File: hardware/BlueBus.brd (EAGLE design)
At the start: 90 x 60 mm, 130 parts, among them Q1 NMOSFET-BSS138K, Q2 PMOSFET-DMP1045UQ, Q3 NMOSFET-BSS138K, X1 CRYSTAL-12MHZ

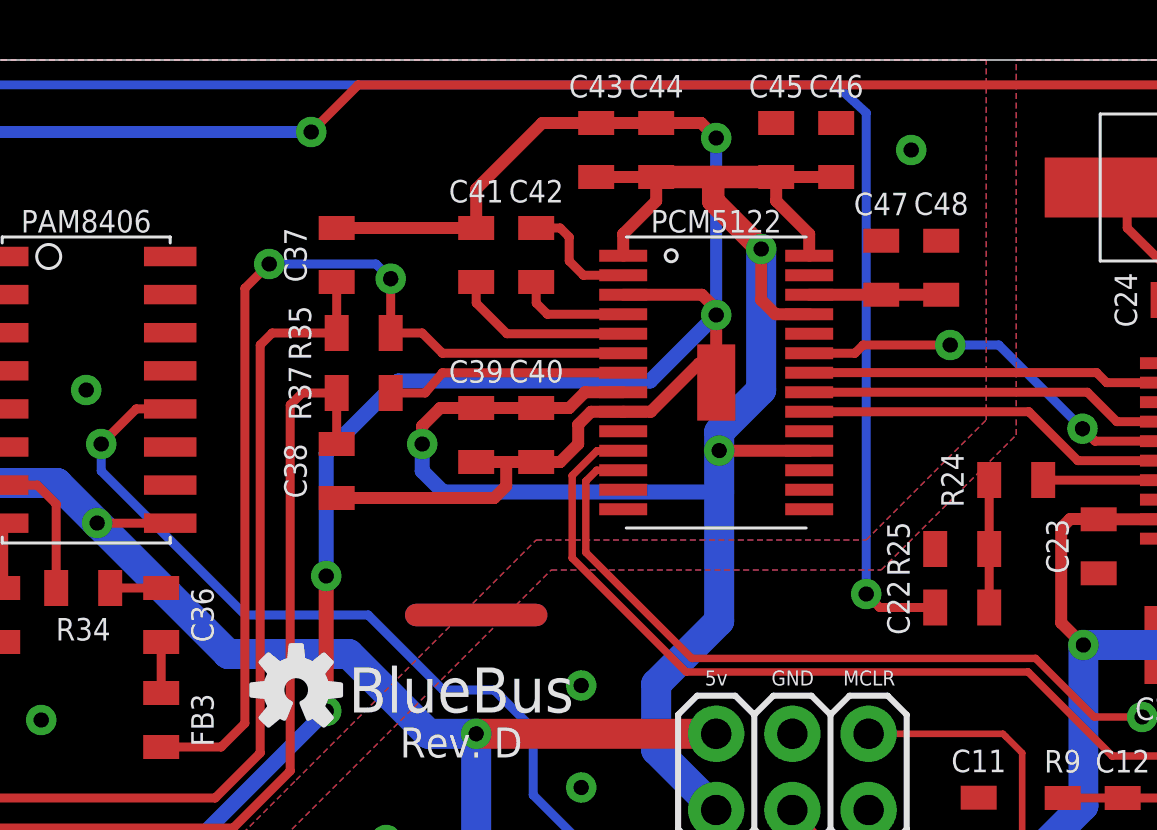
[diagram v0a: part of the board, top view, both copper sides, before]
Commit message: [IMP] hardware: Revision D.1 * Remove errant layers
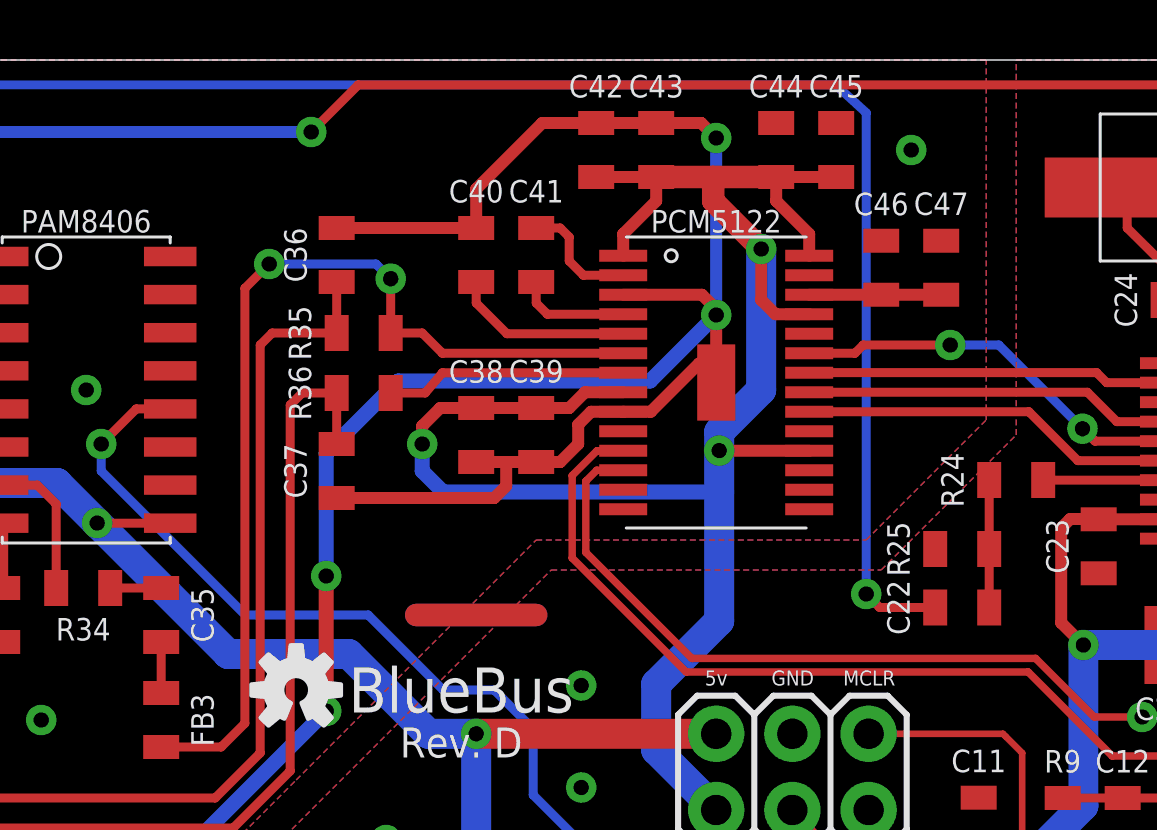
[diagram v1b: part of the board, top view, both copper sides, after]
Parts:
- removed C48: 10uF, Passives:0805
- added C35: 1uF, Passives:0805
- C36: value 1uF -> 9nF
- C38: value 9nF -> 10uF
- C39, C43, C46: value 10uF -> 0.1uF
- C40: value 0.1uF -> 2.2uF
- C42: value 2.2uF -> 10uF
- C45, C47: value 0.1uF -> 10uF
- moved C36 13.4 mm to (29.4, 53.5)
- moved C37 7.20 mm to (29.4, 46.3), turned to 270 degrees
- moved C40 6.32 mm to (34.0, 53.5)
- moved C38 4.80 mm to (34.0, 47.5)
- moved C46 4.20 mm to (47.5, 53.1)
- moved C42 4.03 mm to (38.0, 57.0), turned to 90 degrees
- moved C44 4.00 mm to (44.0, 57.0)
- moved C39 2.00 mm to (36.0, 47.5)
- moved C41 2.00 mm to (36.0, 53.5)
- moved C43 2.00 mm to (40.0, 57.0)
- moved C45 2.00 mm to (46.0, 57.0)
- moved C47 2.00 mm to (49.5, 53.1)
- renumbered R37 to R36
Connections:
- net 3.3V: now also C38.1, C42.1; no longer C40.1, C46.1
- net AGND: now also C36.2, C40.1, C42.2; no longer C40.2, C41.1, C44.2
- net DAC_CAPM: now also C41.2; no longer C42.2
- net DAC_CAPP: now also C41.1; no longer C42.1
- net DAC_LDOO: now also C46.1; no longer C48.1
- net DAC_VNEG: now also C40.2; no longer C41.2
- net GND: now also C44.2; no longer C48.2
- net SPKR_OUT_L: now also C36.1; no longer C37.1
- net SPKR_OUT_R: now also C37.1; no longer C38.1
- net TEL_AMP_IN: now also C35.1; no longer C36.1
- net TEL_AMP_INL_CAP_RES: now also C35.2; no longer C36.2

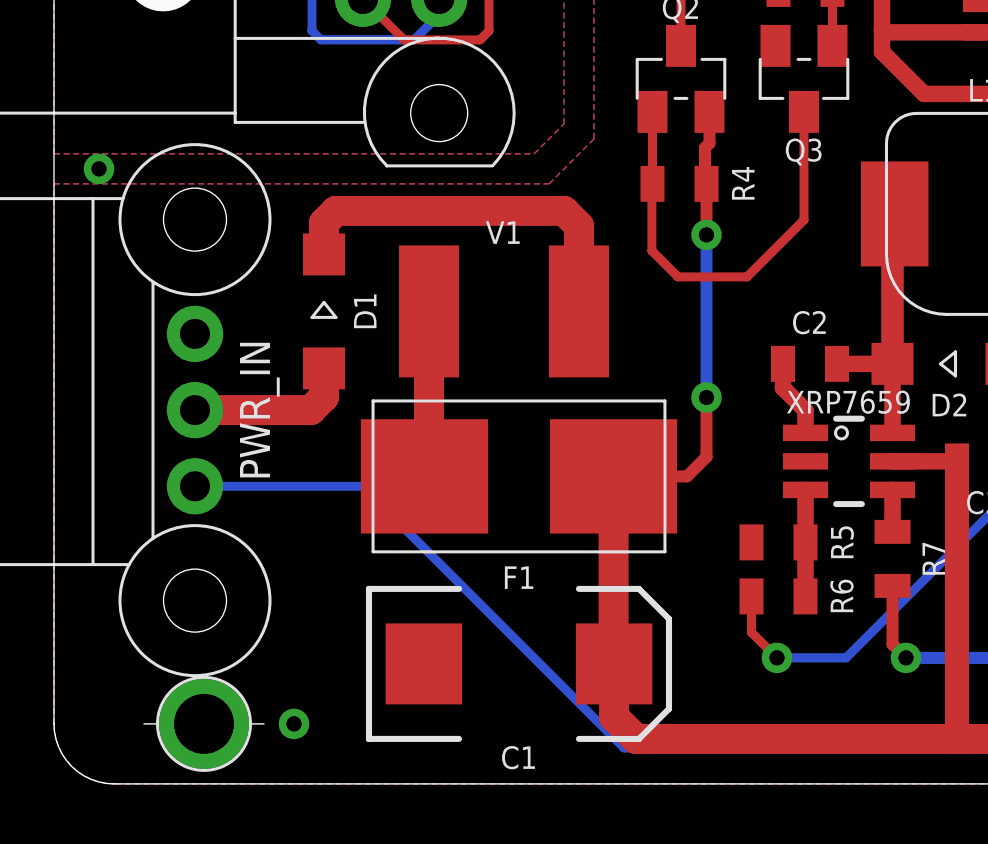
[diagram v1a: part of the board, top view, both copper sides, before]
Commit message: [IMP] hardware: Update Varistor wiring * Improve Schematic drawing for circuit protection
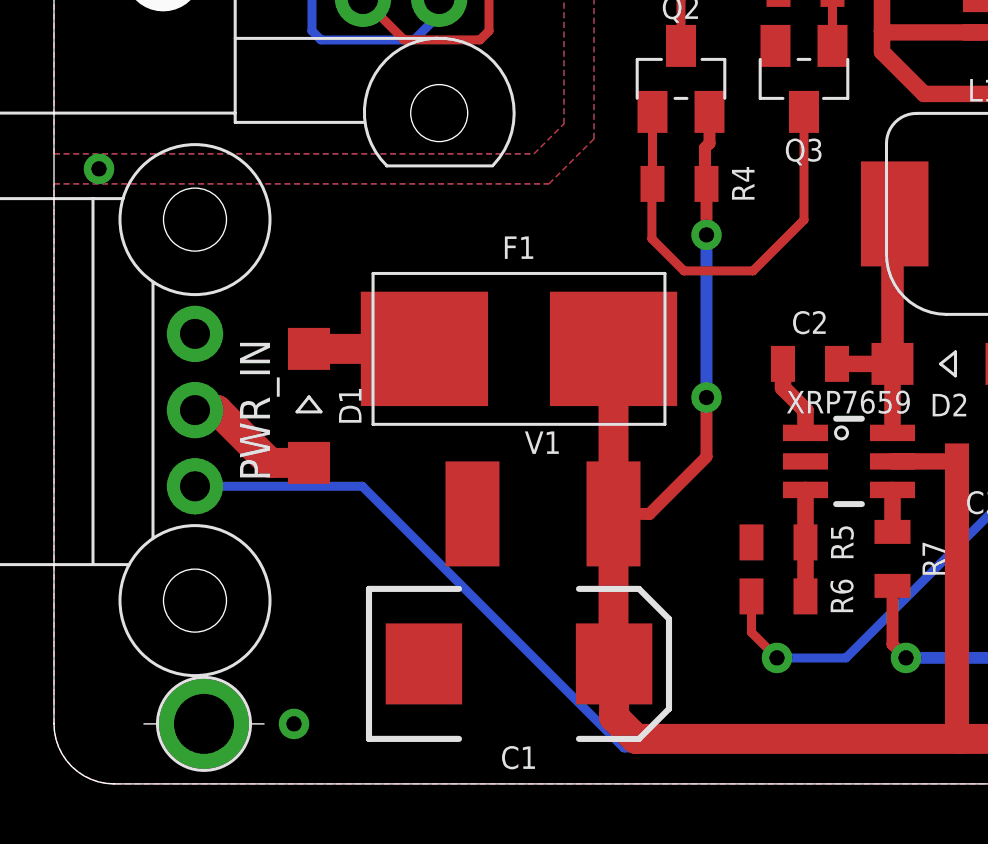
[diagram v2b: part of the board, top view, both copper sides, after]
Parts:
- moved V1 6.87 mm to (16.3, 9.00)
- moved F1 4.25 mm to (15.5, 14.5)
- moved D1 3.19 mm to (8.50, 12.6)
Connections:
- net GND: now also V1.1
- net VIN: no longer V1.1
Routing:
- net VIN: track 94.8 -> 84.2 mm
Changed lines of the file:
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@@
 <layers>
 <layer number="1" name="Top" color="4" fill="1" visible="yes" active="yes"/>
+<layer number="2" name="Route2" color="1" fill="3" visible="no" active="no"/>
+<layer number="3" name="Route3" color="4" fill="3" visible="no" active="yes"/>
+<layer number="4" name="Route4" color="1" fill="4" visible="no" active="yes"/>
+<layer number="5" name="Route5" color="4" fill="4" visible="no" active="yes"/>
+<layer number="6" name="Route6" color="1" fill="8" visible="no" active="yes"/>
+<layer number="7" name="Route7" color="4" fill="8" visible="no" active="yes"/>
+<layer number="8" name="Route8" color="1" fill="2" visible="no" active="yes"/>
+<layer number="9" name="Route9" color="4" fill="2" visible="no" active="yes"/>
+<layer number="10" name="Route10" color="1" fill="7" visible="no" active="yes"/>
+<layer number="11" name="Route11" color="4" fill="7" visible="no" active="yes"/>
+<layer number="12" name="Route12" color="1" fill="5" visible="no" active="yes"/>
+<layer number="13" name="Route13" color="4" fill="5" visible="no" active="yes"/>
+<layer number="14" name="Route14" color="1" fill="6" visible="no" active="yes"/>
+<layer number="15" name="Route15" color="4" fill="6" visible="no" active="no"/>
 <layer number="16" name="Bottom" color="1" fill="1" visible="yes" active="yes"/>
 <layer number="17" name="Pads" color="2" fill="1" visible="yes" active="yes"/>
@@
 <attribute name="VALUE" x="37" y="27.85" size="0.5" layer="27" font="vector" ratio="15" rot="R90" align="top-center"/>
 </element>
-<element name="D1" library="Passives" package="SOD123" value="2A/100V" x="9" y="15.75" smashed="yes" rot="R270">
-<attribute name="MFG" value="STMicroelectronics" x="-45.61" y="-64.26" size="1.778" layer="27" rot="R270" display="off"/>
-<attribute name="NAME" x="10" y="15.75" size="0.75" layer="25" font="vector" ratio="15" rot="R270" align="bottom-center"/>
-<attribute name="PN" value="STPS2H100ZFY" x="-45.61" y="-64.26" size="1.778" layer="27" rot="R270" display="off"/>
-<attribute name="VALUE" x="8" y="15.75" size="0.5" layer="27" font="vector" ratio="15" rot="R270" align="top-center"/>
+<element name="D1" library="Passives" package="SOD123" value="2A/100V" x="8.5" y="12.6" smashed="yes" rot="R270">
+<attribute name="MFG" value="STMicroelectronics" x="-46.11" y="-67.41" size="1.778" layer="27" rot="R270" display="off"/>
+<attribute name="NAME" x="9.5" y="12.6" size="0.75" layer="25" font="vector" ratio="15" rot="R270" align="bottom-center"/>
+<attribute name="PN" value="STPS2H100ZFY" x="-46.11" y="-67.41" size="1.778" layer="27" rot="R270" display="off"/>
+<attribute name="VALUE" x="7.5" y="12.6" size="0.5" layer="27" font="vector" ratio="15" rot="R270" align="top-center"/>
 </element>
 <element name="D2" library="Passives" package="SOD123" value="2A/100V" x="29.85" y="14" smashed="yes">
@@
 <attribute name="VALUE" x="24.5" y="38" size="0.5" layer="27" font="vector" ratio="15" rot="R90" align="top-center"/>
 </element>
-<element name="V1" library="Passives" package="1812" value="V18AUMLA1812H" x="15" y="15.75" smashed="yes">
-<attribute name="NAME" x="15" y="18" size="0.75" layer="25" ratio="18" align="bottom-center"/>
-</element>
-<element name="F1" library="Passives" package="LITTLEFUSE" value="750mA" x="15.5" y="10.25" smashed="yes" rot="R90">
-<attribute name="MFG" value="LITTLEBLOCK" x="15.5" y="10.25" size="1.778" layer="27" rot="R90" display="off"/>
-<attribute name="NAME" x="15.5" y="7.25" size="0.75" layer="25" font="vector" ratio="15" rot="R180" align="bottom-center"/>
-<attribute name="PN" value="0154.750DRT" x="15.5" y="10.25" size="1.778" layer="27" rot="R90" display="off"/>
-<attribute name="VALUE" x="15.5" y="13.25" size="0.5" layer="27" font="vector" ratio="15" rot="R180" align="top-center"/>
+<element name="V1" library="Passives" package="1812" value="V18AUMLA1812H" x="16.3" y="9" smashed="yes">
+<attribute name="NAME" x="16.3" y="11" size="0.75" layer="25" ratio="18" align="bottom-center"/>
+</element>
+<element name="F1" library="Passives" package="LITTLEFUSE" value="750mA" x="15.5" y="14.5" smashed="yes" rot="R90">
+<attribute name="MFG" value="LITTLEBLOCK" x="15.5" y="14.5" size="1.778" layer="27" rot="R90" display="off"/>
+<attribute name="NAME" x="15.5" y="17.5" size="0.75" layer="25" font="vector" ratio="15" rot="R180" align="top-center"/>
+<attribute name="PN" value="0154.750DRT" x="15.5" y="14.5" size="1.778" layer="27" rot="R90" display="off"/>
+<attribute name="VALUE" x="15.5" y="17.5" size="0.5" layer="27" font="vector" ratio="15" rot="R180" align="top-center"/>
 </element>
 <element name="F2" library="Passives" package="1206" value="0468.500NR" x="37.4" y="24.5" smashed="yes">
@@
 <via x="34" y="7.5" extent="1-16" drill="0.51"/>
 <via x="80.8" y="45.5" extent="1-16" drill="0.51"/>
+<contactref element="V1" pad="1"/>
 </signal>
 <signal name="VIN" class="3">
@@
 <wire x1="52.5" y1="2.5" x2="54.55" y2="2.5" width="0.65" layer="1"/>
 <contactref element="C1" pad="A"/>
-<contactref element="D1" pad="C"/>
-<contactref element="V1" pad="1"/>
-<contactref element="F1" pad="OUT"/>
-<contactref element="V1" pad="2"/>
-<contactref element="F1" pad="IN"/>
-<wire x1="18.6515" y1="4.0185" x2="18.67" y2="4" width="1" layer="1"/>
 <wire x1="19.4" y1="1.5" x2="30.2" y2="1.5" width="1" layer="1"/>
-<wire x1="12.5" y1="15.75" x2="12.5" y2="10.4015" width="1" layer="1"/>
-<wire x1="12.5" y1="10.4015" x2="12.3485" y2="10.25" width="1" layer="1"/>
-<wire x1="18.6515" y1="10.25" x2="18.6515" y2="4.0185" width="1" layer="1"/>
 <wire x1="18.67" y1="4" x2="18.67" y2="2.23" width="1" layer="1"/>
 <wire x1="18.67" y1="2.23" x2="19.4" y2="1.5" width="1" layer="1"/>
-<wire x1="8.56" y1="12.46" x2="4.7" y2="12.46" width="1" layer="1"/>
 <wire x1="21.85" y1="22.4" x2="21.85" y2="21.35" width="0.4" layer="1"/>
 <wire x1="21.85" y1="21.35" x2="21.7" y2="21.2" width="0.4" layer="1"/>
@@
 <wire x1="21.75" y1="18.3" x2="21.75" y2="12.88" width="0.4" layer="16"/>
 <via x="21.75" y="12.88" extent="1-16" drill="0.51"/>
-<wire x1="21.75" y1="12.88" x2="21.75" y2="10.9" width="0.4" layer="1"/>
-<wire x1="21.1" y1="10.25" x2="21.75" y2="10.9" width="0.4" layer="1"/>
-<wire x1="18.6515" y1="10.25" x2="21.1" y2="10.25" width="0.4" layer="1"/>
-<wire x1="17.5" y1="15.75" x2="17.5" y2="18.6" width="1" layer="1"/>
-<wire x1="17" y1="19.1" x2="17.5" y2="18.6" width="1" layer="1"/>
-<wire x1="9" y1="17.65" x2="9" y2="18.7" width="1" layer="1"/>
-<wire x1="9.4" y1="19.1" x2="17" y2="19.1" width="1" layer="1"/>
-<wire x1="9" y1="18.7" x2="9.4" y2="19.1" width="1" layer="1"/>
-<wire x1="9" y1="13.85" x2="9" y2="12.9" width="1" layer="1"/>
-<wire x1="9" y1="12.9" x2="8.56" y2="12.46" width="1" layer="1"/>
-<wire x1="9" y1="13.85" x2="9" y2="17.65" width="0" layer="19" extent="1-1"/>
-<wire x1="12.5" y1="15.75" x2="9" y2="17.65" width="0" layer="19" extent="1-1"/>
-<wire x1="21.75" y1="18.3" x2="17.5" y2="15.75" width="0" layer="19" extent="1-1"/>
+<wire x1="21.75" y1="10.9" x2="21.75" y2="12.88" width="0.4" layer="1"/>
+<contactref element="F1" pad="OUT"/>
+<contactref element="V1" pad="2"/>
+<contactref element="D1" pad="C"/>
+<contactref element="F1" pad="IN"/>
+<wire x1="18.6515" y1="14.5" x2="18.6515" y2="9.0015" width="1" layer="1"/>
+<wire x1="18.6515" y1="9.0015" x2="18.65" y2="9" width="1" layer="1"/>
+<wire x1="18.65" y1="9" x2="18.65" y2="4.02" width="1" layer="1"/>
+<wire x1="18.65" y1="4.02" x2="18.67" y2="4" width="1" layer="1"/>
+<wire x1="12.3485" y1="14.5" x2="8.5" y2="14.5" width="1" layer="1"/>
+<wire x1="4.7" y1="12.46" x2="5.44" y2="12.46" width="1" layer="1"/>
+<wire x1="7.2" y1="10.7" x2="8.5" y2="10.7" width="1" layer="1"/>
+<wire x1="5.44" y1="12.46" x2="7.2" y2="10.7" width="1" layer="1"/>
+<wire x1="18.65" y1="9" x2="19.85" y2="9" width="0.4" layer="1"/>
+<wire x1="19.85" y1="9" x2="21.75" y2="10.9" width="0.4" layer="1"/>
+<wire x1="8.5" y1="10.7" x2="8.5" y2="14.5" width="0" layer="19" extent="1-1"/>
+<wire x1="18.6515" y1="14.5" x2="12.3485" y2="14.5" width="0" layer="19" extent="1-1"/>
 </signal>
 <signal name="IBUS" class="4">
@@
 <contactref element="R4" pad="1"/>
 <wire x1="25" y1="22.4" x2="25" y2="18.8" width="0.3" layer="1"/>
-<wire x1="25" y1="18.8" x2="23.1" y2="16.9" width="0.3" layer="1"/>
-<wire x1="23.1" y1="16.9" x2="20.8" y2="16.9" width="0.3" layer="1"/>
-<wire x1="20.8" y1="16.9" x2="19.93" y2="17.77" width="0.3" layer="1"/>
-<wire x1="19.93" y1="17.77" x2="19.93" y2="19.98" width="0.3" layer="1"/>
+<wire x1="25" y1="18.8" x2="23.3" y2="17.1" width="0.3" layer="1"/>
+<wire x1="23.3" y1="17.1" x2="21" y2="17.1" width="0.3" layer="1"/>
+<wire x1="21" y1="17.1" x2="19.93" y2="18.17" width="0.3" layer="1"/>
+<wire x1="19.93" y1="18.17" x2="19.93" y2="19.98" width="0.3" layer="1"/>
 <wire x1="19.93" y1="19.98" x2="19.95" y2="20" width="0.3" layer="1"/>
 <wire x1="19.95" y1="20" x2="19.95" y2="22.4" width="0.3" layer="1"/>
